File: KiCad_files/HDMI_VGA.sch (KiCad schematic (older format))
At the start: 30 parts

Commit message: Added VGA
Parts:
- added J?: DB15_Female_HighDensity_MountingHoles, symbol DB15_Female_HighDensity_MountingHoles
- added R? (x3): 4k, symbol R
- added R? (x3): 2k, symbol R
- added R? (x3): 1k, symbol R
- added R? (x3): 510, symbol R
- added R? (x2): 100, symbol R
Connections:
- net labels added: VGA_B1, VGA_B2, VGA_B3, VGA_B4, VGA_G1, VGA_G2, VGA_G3, VGA_G4, VGA_HS, VGA_R1, VGA_R2, VGA_R3, VGA_R4, VGA_VS
- wire segments 58 -> 102
- no-connect marks 0 -> 5

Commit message: Cleanup for demo/presentation
Merged Config and Debug sheets.
Added GPIO for remaining pins.
Annotations.
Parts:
- removed R?: 10, symbol R
- gave numbers to parts that had none: 44
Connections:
- net labels removed: HDMI_R_SPDIF, HDMI_SPDIF, HDMI_SPDIF_OUT_LS
- wire segments 102 -> 100

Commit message: Added Decoupling Caps?
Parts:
- added J?: HDMI_A_1.4, symbol HDMI_A_1.4
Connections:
- no-connect marks 5 -> 6
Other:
- note removed: "Place HDMI connector here"
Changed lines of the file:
@@
 LIBS:valves
 LIBS:custom
+LIBS:Connector
 LIBS:RASAC-cache
 EELAYER 25 0
@@
 Text GLabel 6000 3300 2    60   Input ~ 0
 HDMI_CLK_N
-Text GLabel 8000 2300 0    60   Input ~ 0
+Text GLabel 8100 1900 0    60   Input ~ 0
 HDMI_D2_P
-Text GLabel 8000 2400 0    60   Input ~ 0
+Text GLabel 8100 2000 0    60   Input ~ 0
 HDMI_D2_N
-Text GLabel 8000 2600 0    60   Input ~ 0
+Text GLabel 8100 2100 0    60   Input ~ 0
 HDMI_D1_P
-Text GLabel 8000 2700 0    60   Input ~ 0
+Text GLabel 8100 2200 0    60   Input ~ 0
 HDMI_D1_N
-Text GLabel 8000 2900 0    60   Input ~ 0
+Text GLabel 8100 2300 0    60   Input ~ 0
 HDMI_D0_P
-Text GLabel 8000 3000 0    60   Input ~ 0
+Text GLabel 8100 2400 0    60   Input ~ 0
 HDMI_D0_N
-Text GLabel 8000 3200 0    60   Input ~ 0
+Text GLabel 8100 2500 0    60   Input ~ 0
 HDMI_CLK_P
-Text GLabel 8000 3300 0    60   Input ~ 0
+Text GLabel 8100 2600 0    60   Input ~ 0
 HDMI_CLK_N
-Text Notes 8150 2800 0    60   ~ 0
-Place HDMI connector here
-Text GLabel 8000 2100 0    60   Input ~ 0
+Text GLabel 8500 1600 1    60   Input ~ 0
 VCC5V5
 $Comp
 L GND #PWR112
 U 1 1 5C18DC55
-P 8000 3500
-F 0 "#PWR112" H 8000 3250 50  0001 C CNN
-F 1 "GND" H 8000 3350 50  0001 C CNN
-F 2 "" H 8000 3500 50  0001 C CNN
-F 3 "" H 8000 3500 50  0001 C CNN
-	1    8000 3500
-	0    1    1    0
+P 8700 3800
+F 0 "#PWR112" H 8700 3550 50  0001 C CNN
+F 1 "GND" H 8700 3650 50  0001 C CNN
+F 2 "" H 8700 3800 50  0001 C CNN
+F 3 "" H 8700 3800 50  0001 C CNN
+	1    8700 3800
+	1    0    0    -1
 $EndComp
 $Comp
@@
 Text GLabel 5000 4600 3    60   Input ~ 0
 HDMI_INT
+NoConn ~ 5200 1500
+$Comp
+L HDMI_A_1.4 J?
+U 1 1 5C47F6C9
+P 8500 2700
+F 0 "J?" H 8250 3750 50  0000 C CNN
+F 1 "HDMI_A_1.4" H 8900 3750 50  0000 C CNN
+F 2 "" H 8525 2700 50  0001 C CNN
+F 3 "" H 8525 2700 50  0001 C CNN
+	1    8500 2700
+	1    0    0    -1
+$EndComp
 $EndSCHEMATC

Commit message: Cleanup + Update to KiCad 5.0 + DDR2
Updated to KiCad 5, which re-organized libraries, so corrected them to not need RASAC-rescue.lib.
Also cleaned up some stuff.
DDR4 has been removed and in place will be DDR2.
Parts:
- J7: symbol TFP410 -> custom:TFP410
- J8: symbol DB15_Female_HighDensity_MountingHoles -> Connector:DB15_Female_HighDensity_MountingHoles
- J?: symbol HDMI_A_1.4 -> Connector:HDMI_A_1.4
- R32, R33, R34, R35, R36, R37, R38, R39, R40, R41, R42, R43, R44, R45, R46, R47, R48, R49, R50, R51, R52, R53, R54, R55, R56, R57, R58, R59, R60, R61, R62, R63, R64, R65, R66, R67, R68, R69, R70, R71, R72, R73: symbol R -> Device:R
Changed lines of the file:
@@
-EESchema Schematic File Version 2
-LIBS:power
-LIBS:device
-LIBS:switches
-LIBS:relays
-LIBS:motors
-LIBS:transistors
-LIBS:conn
-LIBS:linear
-LIBS:regul
-LIBS:74xx
-LIBS:cmos4000
-LIBS:adc-dac
-LIBS:memory
-LIBS:xilinx
-LIBS:microcontrollers
-LIBS:dsp
-LIBS:microchip
-LIBS:analog_switches
-LIBS:motorola
-LIBS:texas
-LIBS:intel
-LIBS:audio
-LIBS:interface
-LIBS:digital-audio
-LIBS:philips
-LIBS:display
-LIBS:cypress
-LIBS:siliconi
-LIBS:opto
-LIBS:atmel
-LIBS:contrib
-LIBS:valves
-LIBS:custom
-LIBS:Connector
+EESchema Schematic File Version 4
 LIBS:RASAC-cache
-EELAYER 25 0
+EELAYER 26 0
 EELAYER END
 $Descr A4 11693 8268
@@
 HDMI_DE
 $Comp
-L R R32
+L Device:R R32
 U 1 1 5C18441D
 P 1850 4500
@@
 $EndComp
 $Comp
-L R R46
+L Device:R R46
 U 1 1 5C18449A
 P 2150 4600
@@
 $EndComp
 $Comp
-L R R33
+L Device:R R33
 U 1 1 5C18454B
 P 1850 4700
@@
 $EndComp
 $Comp
-L R R47
+L Device:R R47
 U 1 1 5C184551
 P 2150 4800
@@
 $EndComp
 $Comp
-L R R34
+L Device:R R34
 U 1 1 5C184617
 P 1850 4900
@@
 $EndComp
 $Comp
-L R R48
+L Device:R R48
 U 1 1 5C18461D
 P 2150 5000
@@
 $EndComp
 $Comp
-L R R35
+L Device:R R35
 U 1 1 5C184627
 P 1850 5100
@@
 $EndComp
 $Comp
-L R R49
+L Device:R R49
 U 1 1 5C18462D
 P 2150 5200
@@
 $EndComp
 $Comp
-L R R36
+L Device:R R36
 U 1 1 5C1846CF
 P 1850 5300
@@
 $EndComp
 $Comp
-L R R50
+L Device:R R50
 U 1 1 5C1846D5
 P 2150 5400
@@
 $EndComp
 $Comp
-L R R37
+L Device:R R37
 U 1 1 5C1846DF
 P 1850 5500
@@
 $EndComp
 $Comp
-L R R51
+L Device:R R51
 U 1 1 5C1846E5
 P 2150 5600
@@
 $EndComp
 $Comp
-L R R38
+L Device:R R38
 U 1 1 5C1846EF
 P 1850 5700
@@
 $EndComp
 $Comp
-L R R52
+L Device:R R52
 U 1 1 5C1846F5
 P 2150 5800
@@
 $EndComp
 $Comp
-L R R39
+L Device:R R39
 U 1 1 5C1846FF
 P 1850 5900
@@
 $EndComp
 $Comp
-L R R53
+L Device:R R53
 U 1 1 5C184705
 P 2150 6000
@@
 $EndComp
 $Comp
-L R R40
+L Device:R R40
 U 1 1 5C18487F
 P 1850 6100
@@
 $EndComp
 $Comp
-L R R54
+L Device:R R54
 U 1 1 5C184885
 P 2150 6200
@@
 $EndComp
 $Comp
-L R R41
+L Device:R R41
 U 1 1 5C18488F
 P 1850 6300
@@
 $EndComp
 $Comp
-L R R55
+L Device:R R55
 U 1 1 5C184895
 P 2150 6400
@@
 $EndComp
 $Comp
-L R R42
+L Device:R R42
 U 1 1 5C18489F
 P 1850 6500
@@
 $EndComp
 $Comp
-L R R56
+L Device:R R56
 U 1 1 5C1848A5
 P 2150 6600
@@
 $EndComp
 $Comp
-L R R43
+L Device:R R43
 U 1 1 5C1848AF
 P 1850 6700
@@
 $EndComp
 $Comp
-L R R57
+L Device:R R57
 U 1 1 5C1848B5
 P 2150 6800
@@
 $EndComp
 $Comp
-L R R44
+L Device:R R44
 U 1 1 5C1848BF
 P 1850 6900
@@
 $EndComp
 $Comp
-L R R58
+L Device:R R58
 U 1 1 5C1848C5
 P 2150 7000
@@
 $EndComp
 $Comp
-L R R45
+L Device:R R45
 U 1 1 5C1848CF
 P 1850 7100
@@
 $EndComp
 $Comp
-L R R59
+L Device:R R59
 U 1 1 5C1848D5
 P 2150 7200
@@
 Page 4 of TFP410 Datasheet
 $Comp
-L GND #PWR104
+L power:GND #PWR0104
 U 1 1 5C189728
 P 3100 2900
-F 0 "#PWR104" H 3100 2650 50  0001 C CNN
+F 0 "#PWR0104" H 3100 2650 50  0001 C CNN
 F 1 "GND" H 3100 2750 50  0001 C CNN
 F 2 "" H 3100 2900 50  0001 C CNN
@@
 $EndComp
 $Comp
-L GND #PWR105
+L power:GND #PWR0105
 U 1 1 5C18B4D7
 P 3100 3700
-F 0 "#PWR105" H 3100 3450 50  0001 C CNN
+F 0 "#PWR0105" H 3100 3450 50  0001 C CNN
 F 1 "GND" H 3100 3550 50  0001 C CNN
 F 2 "" H 3100 3700 50  0001 C CNN
@@
 VCC3V3
 $Comp
-L GND #PWR106
+L power:GND #PWR0106
 U 1 1 5C18B837
 P 3800 1500
-F 0 "#PWR106" H 3800 1250 50  0001 C CNN
+F 0 "#PWR0106" H 3800 1250 50  0001 C CNN
 F 1 "GND" H 3800 1350 50  0001 C CNN
 F 2 "" H 3800 1500 50  0001 C CNN
@@
 $EndComp
 $Comp
-L GND #PWR108
+L power:GND #PWR0108
 U 1 1 5C18B89C
 P 6000 2200
-F 0 "#PWR108" H 6000 1950 50  0001 C CNN
+F 0 "#PWR0108" H 6000 1950 50  0001 C CNN
 F 1 "GND" H 6000 2050 50  0001 C CNN
 F 2 "" H 6000 2200 50  0001 C CNN
@@
 $EndComp
 $Comp
-L GND #PWR111
+L power:GND #PWR0111
 U 1 1 5C18B943
 P 6000 3700
-F 0 "#PWR111" H 6000 3450 50  0001 C CNN
+F 0 "#PWR0111" H 6000 3450 50  0001 C CNN
 F 1 "GND" H 6000 3550 50  0001 C CNN
 F 2 "" H 6000 3700 50  0001 C CNN
@@
 VCC3V3
 $Comp
-L GND #PWR110
+L power:GND #PWR0110
 U 1 1 5C18BA5F
 P 6000 3400
-F 0 "#PWR110" H 6000 3150 50  0001 C CNN
+F 0 "#PWR0110" H 6000 3150 50  0001 C CNN
 F 1 "GND" H 6000 3250 50  0001 C CNN
 F 2 "" H 6000 3400 50  0001 C CNN
@@
 VCC3V3
 $Comp
-L TFP410 J7
+L custom:TFP410 J7
 U 1 1 5C18C3A5
 P 4550 2950
@@
 $EndComp
 $Comp
-L GND #PWR109
+L power:GND #PWR0109
 U 1 1 5C18C420
 P 6000 2800
-F 0 "#PWR109" H 6000 2550 50  0001 C CNN
+F 0 "#PWR0109" H 6000 2550 50  0001 C CNN
 F 1 "GND" H 6000 2650 50  0001 C CNN
 F 2 "" H 6000 2800 50  0001 C CNN
@@
 $EndComp
 $Comp
-L GND #PWR107
+L power:GND #PWR0107
 U 1 1 5C18C485
 P 5300 4400
-F 0 "#PWR107" H 5300 4150 50  0001 C CNN
+F 0 "#PWR0107" H 5300 4150 50  0001 C CNN
 F 1 "GND" H 5300 4250 50  0001 C CNN
 F 2 "" H 5300 4400 50  0001 C CNN
@@
 VCC5V5
 $Comp
-L GND #PWR112
+L power:GND #PWR0112
 U 1 1 5C18DC55
 P 8700 3800
-F 0 "#PWR112" H 8700 3550 50  0001 C CNN
+F 0 "#PWR0112" H 8700 3550 50  0001 C CNN
 F 1 "GND" H 8700 3650 50  0001 C CNN
 F 2 "" H 8700 3800 50  0001 C CNN
@@
 $EndComp
 $Comp
-L DB15_Female_HighDensity_MountingHoles J8
+L Connector:DB15_Female_HighDensity_MountingHoles J8
 U 1 1 5C18B39F
 P 8900 5000
@@
 VGA_VS
 $Comp
-L R R60
+L Device:R R60
 U 1 1 5C18C1A3
 P 7900 4300
@@
 $EndComp
 $Comp
-L R R66
+L Device:R R66
 U 1 1 5C18C563
 P 8200 4400
@@
 $EndComp
 $Comp
-L R R61
+L Device:R R61
 U 1 1 5C18C88C
 P 7900 4500
@@
 $EndComp
 $Comp
-L R R67
+L Device:R R67
 U 1 1 5C18C892
 P 8200 4600
@@
 $EndComp
 $Comp
-L R R62
+L Device:R R62
 U 1 1 5C18CA2A
 P 7900 4800
@@
 $EndComp
 $Comp
-L R R68
+L Device:R R68
 U 1 1 5C18CA30
 P 8200 4900
@@
 $EndComp
 $Comp
-L R R63
+L Device:R R63
 U 1 1 5C18CA3A
 P 7900 5000
@@
 $EndComp
 $Comp
-L R R69
+L Device:R R69
 U 1 1 5C18CA40
 P 8200 5100
@@
 $EndComp
 $Comp
-L R R64
+L Device:R R64
 U 1 1 5C18CBB4
 P 7900 5300
@@
 $EndComp
 $Comp
-L R R70
+L Device:R R70
 U 1 1 5C18CBBA
 P 8200 5400
@@
 $EndComp
 $Comp
-L R R65
+L Device:R R65
 U 1 1 5C18CBC4
 P 7900 5500
@@
 $EndComp
 $Comp
-L R R71
+L Device:R R71
 U 1 1 5C18CBCA
 P 8200 5600
@@
 $EndComp
 $Comp
-L R R73
+L Device:R R73
 U 1 1 5C18CCA0
 P 9800 5050
@@
 $EndComp
 $Comp
-L R R72
+L Device:R R72
 U 1 1 5C18CCA6
 P 9500 5150
@@
 Connection ~ 8550 5400
 $Comp
-L GND #PWR113
+L power:GND #PWR0113
 U 1 1 5C18E2D3
 P 8900 5700
-F 0 "#PWR113" H 8900 5450 50  0001 C CNN
+F 0 "#PWR0113" H 8900 5450 50  0001 C CNN
 F 1 "GND" H 8900 5550 50  0001 C CNN
 F 2 "" H 8900 5700 50  0001 C CNN
@@
 NoConn ~ 5200 1500
 $Comp
-L HDMI_A_1.4 J?
+L Connector:HDMI_A_1.4 J?
 U 1 1 5C47F6C9
 P 8500 2700

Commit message: Minor fixes
Still fixing from KiCad update
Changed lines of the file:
@@
 	8450 4500 8050 4500
 Wire Wire Line
-	8350 4600 8600 4600
+	8350 4600 8450 4600
 Wire Wire Line
 	7750 4800 7650 4800
@@
 	7650 4900 8050 4900
 Wire Wire Line
-	8050 4800 8600 4800
+	8050 4800 8450 4800
 Wire Wire Line
 	8350 4900 8450 4900
@@
 	7650 5400 8050 5400
 Wire Wire Line
-	8050 5300 8500 5300
+	8050 5300 8450 5300
 Wire Wire Line
 	8350 5400 8450 5400
@@
 	9250 5200 9200 5200
 Wire Wire Line
-	8450 4300 8450 4600
+	8450 4300 8450 4400
 Connection ~ 8450 4400
 Connection ~ 8450 4500
 Wire Wire Line
-	8450 4800 8450 5100
+	8450 4800 8450 4900
 Connection ~ 8450 4900
 Connection ~ 8450 5000
 Wire Wire Line
-	8450 5300 8450 5600
+	8450 5300 8450 5400
 Connection ~ 8450 5400
 Connection ~ 8450 5500
@@
 	8600 4500 8550 4500
 Wire Wire Line
-	8550 4500 8550 5700
+	8550 4500 8550 4700
 Wire Wire Line
 	8550 4700 8600 4700
@@
 	1    0    0    -1
 $EndComp
+Wire Wire Line
+	8450 4400 8450 4500
+Wire Wire Line
+	8450 4500 8450 4600
+Wire Wire Line
+	8450 4900 8450 5000
+Wire Wire Line
+	8450 5000 8450 5100
+Wire Wire Line
+	8450 5400 8450 5500
+Wire Wire Line
+	8450 5500 8450 5600
+Wire Wire Line
+	8450 4600 8600 4600
+Wire Wire Line
+	8450 4800 8600 4800
+Wire Wire Line
+	8450 5300 8500 5300
+Wire Wire Line
+	8550 4700 8550 4900
+Wire Wire Line
+	8550 4900 8550 5300
+Wire Wire Line
+	8550 5300 8550 5400
+Wire Wire Line
+	8550 5400 8550 5700
 $EndSCHEMATC

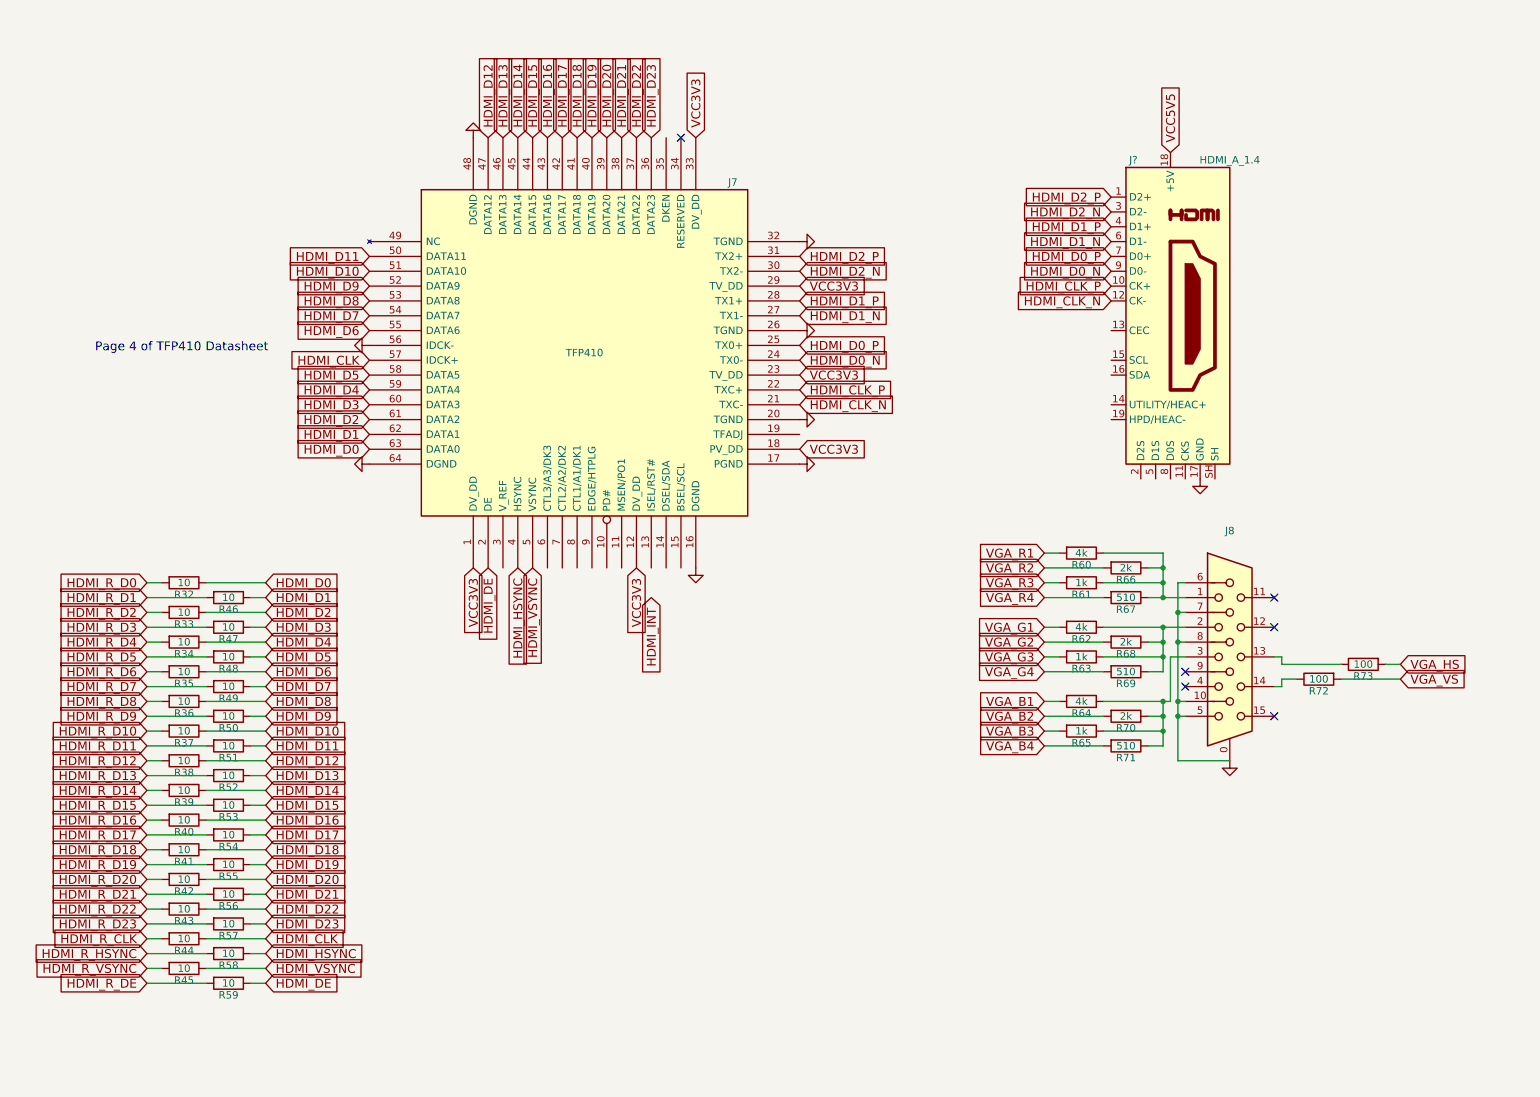
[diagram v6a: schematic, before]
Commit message: Added TPD12S521 Port Protection for HDMI
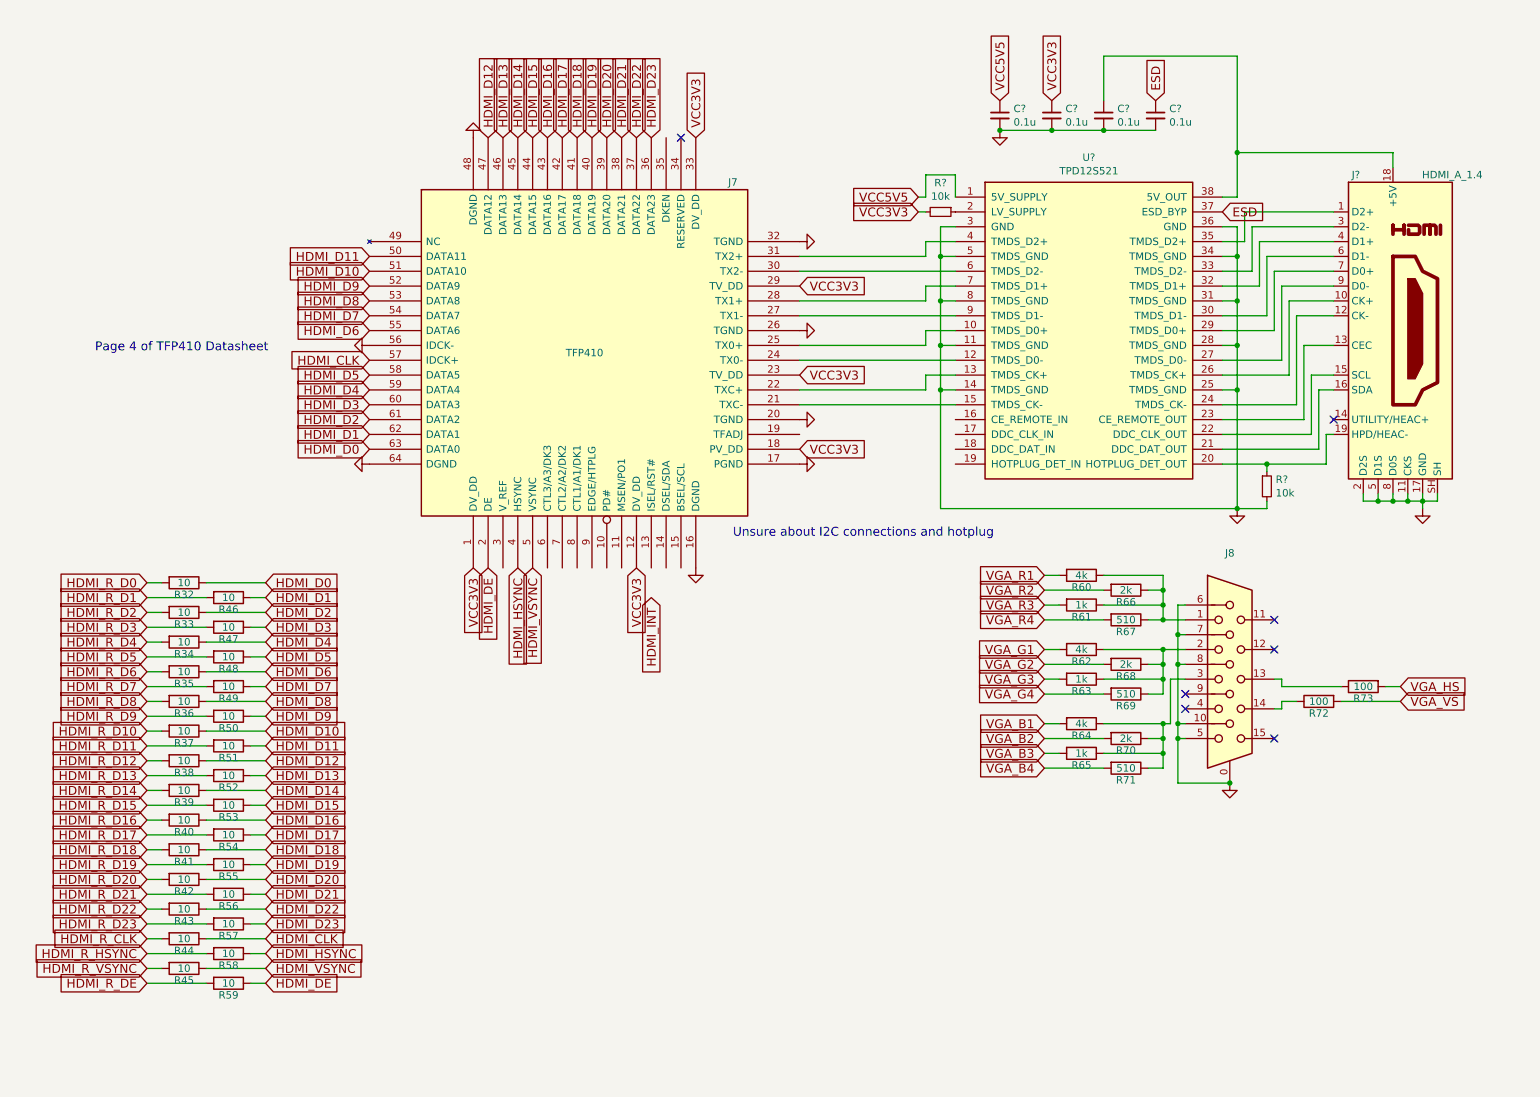
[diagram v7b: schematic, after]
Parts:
- added C? (x4): 0.1u, symbol Device:C_Small
- added R? (x2): 10k, symbol Device:R_Small
- added U?: TPD12S521, symbol custom:TPD12S521
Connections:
- net GND: now also J?.11 (CKS), J?.2 (D2S), J?.5 (D1S), J?.8 (D0S), J?.SH, C?.2, C?.2, C?.2, C?.2, R?.2, U?.11 (TMDS_GND), U?.14 (TMDS_GND), U?.25 (TMDS_GND), U?.28 (TMDS_GND), U?.3 (GND), U?.31 (TMDS_GND), U?.34 (TMDS_GND), U?.36 (GND), U?.5 (TMDS_GND), U?.8 (TMDS_GND)
- net VCC3V3: now also C?.1, R?.2
- net VCC5V5: now also C?.1, U?.1 (5V_SUPPLY); no longer J?.18 (+5V)
- net at J?.13 (CEC): now also U?.23 (CE_REMOTE_OUT)
- net at J?.15 (SCL): now also U?.22 (DDC_CLK_OUT)
- net at J?.16 (SDA): now also U?.21 (DDC_DAT_OUT)
- net at J?.19 (HPD/HEAC-): now also R?.1, U?.20 (HOTPLUG_DET_OUT)
- net HDMI_CLK_N: no longer names the net of J7.21 (TXC-)
- net HDMI_CLK_N: now also U?.15 (TMDS_CK-); no longer J?.12 (CK-)
- net HDMI_CLK_P: no longer names the net of J7.22 (TXC+)
- net HDMI_CLK_P: now also U?.13 (TMDS_CK+); no longer J?.10 (CK+)
- net HDMI_D0_N: no longer names the net of J7.24 (TX0-)
- net HDMI_D0_N: now also U?.12 (TMDS_D0-); no longer J?.9 (D0-)
- net HDMI_D0_P: no longer names the net of J7.25 (TX0+)
- net HDMI_D0_P: now also U?.10 (TMDS_D0+); no longer J?.7 (D0+)
- net HDMI_D1_N: no longer names the net of J7.27 (TX1-)
- net HDMI_D1_N: now also U?.9 (TMDS_D1-); no longer J?.6 (D1-)
- net HDMI_D1_P: no longer names the net of J7.28 (TX1+)
- net HDMI_D1_P: now also U?.7 (TMDS_D1+); no longer J?.4 (D1+)
- net HDMI_D2_N: no longer names the net of J7.30 (TX2-)
- net HDMI_D2_N: now also U?.6 (TMDS_D2-); no longer J?.3 (D2-)
- net HDMI_D2_P: no longer names the net of J7.31 (TX2+)
- net HDMI_D2_P: now also U?.4 (TMDS_D2+); no longer J?.1 (D2+)
- new net: J?.1 (D2+), U?.35 (TMDS_D2+)
- new net: J?.10 (CK+), U?.26 (TMDS_CK+)
- new net: J?.12 (CK-), U?.24 (TMDS_CK-)
- new net: C?.1, J?.18 (+5V), U?.38 (5V_OUT)
- new net: J?.3 (D2-), U?.33 (TMDS_D2-)
- new net: J?.4 (D1+), U?.32 (TMDS_D1+)
- new net: J?.6 (D1-), U?.30 (TMDS_D1-)
- new net: J?.7 (D0+), U?.29 (TMDS_D0+)
- new net: J?.9 (D0-), U?.27 (TMDS_D0-)
- new net: R?.1, U?.2 (LV_SUPPLY)
- new net ESD: C?.1, U?.37 (ESD_BYP)
- no-connect marks 6 -> 7
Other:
- note added: "Unsure about I2C connections and hotplug"
- moved on the sheet: J8, J?, R60, R61, R62, R63, R64, R65, R66, R67, R68, R69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
